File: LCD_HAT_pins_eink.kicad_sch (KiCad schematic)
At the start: 32 parts, among them J1 Qwiic, J2 LCD, J3 PWR_JUMPER, J4 PWR_JUMPER, J5 AFC24-S24FIC-00, Q1 Si1308, SW1 SW_Push, SW2 SW_Push, U1 SeeeduinoXIAO

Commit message: Rework routing
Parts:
- removed J4: PWR_JUMPER, Connector_PinHeader_2.54mm:PinHeader_1x02_P2.54mm_Vertical, symbol Connector:Conn_01x02_Pin
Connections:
- net +3.3V: now also J1.2 (Pin_2)
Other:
- title: Feather and Nano to LCD HAT -> Feather and Nano to LCD HAT + 24 pins SPI Eink
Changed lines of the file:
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@@
 	(paper "A4")
 	(title_block
-		(title "Feather and Nano to LCD HAT")
+		(title "Feather and Nano to LCD HAT + 24 pins SPI Eink")
 		(date "2023-01-30")
 		(rev "1.0")
 		(company "BitBank Software, Inc.")
-		(comment 1 "A convenient board to test SPI LCDs")
+		(comment 1 "A convenient board to test SPI LCDs and Eink")
+		(comment 2 "Fork of original idea by FASANI CORP.")
 	)
 	(text "PREVGL"
@@
 	(wire
 		(pts
-			(xy 26.67 107.95) (xy 40.64 107.95)
-		)
-		(stroke
-			(width 0)
-			(type default)
-		)
-	)
-	(wire
-		(pts
 			(xy 248.285 78.105) (xy 250.825 78.105)
 		)
@@
 	(wire
 		(pts
-			(xy 26.67 105.41) (xy 35.56 105.41)
-		)
-		(stroke
-			(width 0)
-			(type default)
-		)
-	)
-	(wire
-		(pts
 			(xy 31.75 82.55) (xy 54.61 82.55)
 		)
@@
 	(wire
 		(pts
+			(xy 35.56 92.075) (xy 39.37 92.075)
+		)
+		(stroke
+			(width 0)
+			(type default)
+		)
+	)
+	(wire
+		(pts
 			(xy 58.42 52.07) (xy 86.36 52.07)
 		)
@@
 	(wire
 		(pts
-			(xy 234.315 55.245) (xy 234.315 56.515)
+			(xy 35.56 87.63) (xy 35.56 92.075)
 		)
 		(stroke
@@
 	(wire
 		(pts
-			(xy 257.175 99.695) (xy 264.795 99.695)
+			(xy 234.315 55.245) (xy 234.315 56.515)
 		)
 		(stroke
@@
 	(wire
 		(pts
-			(xy 134.62 100.33) (xy 49.53 100.33)
+			(xy 257.175 99.695) (xy 264.795 99.695)
 		)
 		(stroke
@@
 	(wire
 		(pts
-			(xy 91.44 64.77) (xy 101.6 64.77)
+			(xy 134.62 100.33) (xy 49.53 100.33)
 		)
 		(stroke
@@
 	(wire
 		(pts
-			(xy 101.6 59.69) (xy 101.6 60.96)
+			(xy 91.44 64.77) (xy 101.6 64.77)
 		)
 		(stroke
@@
 	(wire
 		(pts
-			(xy 97.79 36.83) (xy 161.29 36.83)
+			(xy 101.6 59.69) (xy 101.6 60.96)
 		)
 		(stroke
@@
 	(wire
 		(pts
-			(xy 35.56 87.63) (xy 35.56 105.41)
+			(xy 97.79 36.83) (xy 161.29 36.83)
 		)
 		(stroke
@@
 	(symbol
 		(lib_id "power:+3.3V")
-		(at 40.64 107.95 0)
+		(at 39.37 92.075 0)
 		(unit 1)
 		(exclude_from_sim no)
@@
 		(fields_autoplaced yes)
 		(property "Reference" "#PWR02"
-			(at 40.64 111.76 0)
+			(at 39.37 95.885 0)
 			(effects
 				(font
@@
 		)
 		(property "Value" "+3.3V"
-			(at 40.64 102.87 0)
+			(at 39.37 86.995 0)
 			(effects
 				(font
@@
 		)
 		(property "Footprint" ""
-			(at 40.64 107.95 0)
+			(at 39.37 92.075 0)
 			(effects
 				(font
@@
 		)
 		(property "Datasheet" ""
-			(at 40.64 107.95 0)
+			(at 39.37 92.075 0)
 			(effects
 				(font
@@
 		)
 		(property "Description" ""
-			(at 40.64 107.95 0)
+			(at 39.37 92.075 0)
 			(effects
 				(font
@@
 					(unit 1)
 				)
-			)
-		)
-	)
-	(symbol
-		(lib_id "Connector:Conn_01x02_Pin")
-		(at 21.59 105.41 0)
-		(unit 1)
-		(exclude_from_sim no)
-		(in_bom yes)
-		(on_board yes)
-		(dnp no)
-		(fields_autoplaced yes)
-		(property "Reference" "J4"
-			(at 22.225 101.6 0)
-			(effects
-				(font
-					(size 1.27 1.27)
-				)
-			)
-		)
-		(property "Value" "PWR_JUMPER"
-			(at 22.225 104.14 0)
-			(effects
-				(font
-					(size 1.27 1.27)
-				)
-			)
-		)
-		(property "Footprint" "Connector_PinHeader_2.54mm:PinHeader_1x02_P2.54mm_Vertical"
-			(at 21.59 105.41 0)
-			(effects
-				(font
-					(size 1.27 1.27)
-				)
-				(hide yes)
-			)
-		)
-		(property "Datasheet" "~"
-			(at 21.59 105.41 0)
-			(effects
-				(font
-					(size 1.27 1.27)
-				)
-				(hide yes)
-			)
-		)
-		(property "Description" ""
-			(at 21.59 105.41 0)
-			(effects
-				(font
-					(size 1.27 1.27)
-				)
-			)
-		)
-		(pin "1"
-		)
-		(pin "2"
-		)
-		(instances
-			(project "LCD_HAT"
-				(path "/9ace1ea2-fe32-42b9-a35c-4c1c5b2f3f56"
-					(reference "J4")
-					(unit 1)
-				)

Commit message: FAB Files 1.0
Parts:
- removed J3: PWR_JUMPER, Connector_PinHeader_2.54mm:PinHeader_1x02_P2.54mm_Vertical, symbol Connector:Conn_01x02_Pin
- A1, A2, U1: now left out of the parts list
- J1: LCSC (none) -> C160404
- J5: LCSC (none) -> C262292
- R1, R2: LCSC (none) -> C25804
- R3: LCSC (none) -> C245058
- SW1, SW2: LCSC (none) -> C19190908
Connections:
- net +3.3V: now also J2.2 (Pin_2)
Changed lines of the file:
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@@
 	(wire
 		(pts
-			(xy 163.83 60.96) (xy 163.83 49.53)
+			(xy 163.83 40.64) (xy 163.83 60.96)
 		)
 		(stroke
@@
 	(wire
 		(pts
-			(xy 163.83 46.99) (xy 163.83 40.64)
-		)
-		(stroke
-			(width 0)
-			(type default)
-		)
-	)
-	(wire
-		(pts
 			(xy 146.05 68.58) (xy 167.64 68.58)
 		)
@@
 	(wire
 		(pts
-			(xy 165.1 46.99) (xy 163.83 46.99)
-		)
-		(stroke
-			(width 0)
-			(type default)
-		)
-	)
-	(wire
-		(pts
 			(xy 101.6 54.61) (xy 93.98 54.61)
 		)
@@
 	(wire
 		(pts
-			(xy 163.83 49.53) (xy 165.1 49.53)
-		)
-		(stroke
-			(width 0)
-			(type default)
-		)
-	)
-	(wire
-		(pts
 			(xy 82.55 115.57) (xy 82.55 109.22)
 		)
@@
 			)
 		)
+		(property "LCSC" "C19190908"
+			(at 100.33 115.57 0)
+			(effects
+				(font
+					(size 1.27 1.27)
+				)
+				(hide yes)
+			)
+		)
 		(pin "1"
 		)
@@
 		(unit 1)
 		(exclude_from_sim no)
-		(in_bom yes)
+		(in_bom no)
 		(on_board yes)
 		(dnp no)
@@
 	)
 	(symbol
-		(lib_id "Connector:Conn_01x02_Pin")
-		(at 170.18 49.53 180)
-		(unit 1)
-		(exclude_from_sim no)
-		(in_bom yes)
-		(on_board yes)
-		(dnp no)
-		(fields_autoplaced yes)
-		(property "Reference" "J3"
-			(at 171.45 47.625 0)
-			(effects
-				(font
-					(size 1.27 1.27)
-				)
-				(justify right)
-			)
-		)
-		(property "Value" "PWR_JUMPER"
-			(at 171.45 50.165 0)
-			(effects
-				(font
-					(size 1.27 1.27)
-				)
-				(justify right)
-			)
-		)
-		(property "Footprint" "Connector_PinHeader_2.54mm:PinHeader_1x02_P2.54mm_Vertical"
-			(at 170.18 49.53 0)
-			(effects
-				(font
-					(size 1.27 1.27)
-				)
-				(hide yes)
-			)
-		)
-		(property "Datasheet" "~"
-			(at 170.18 49.53 0)
-			(effects
-				(font
-					(size 1.27 1.27)
-				)
-				(hide yes)
-			)
-		)
-		(property "Description" ""
-			(at 170.18 49.53 0)
-			(effects
-				(font
-					(size 1.27 1.27)
-				)
-			)
-		)
-		(pin "1"
-		)
-		(pin "2"
-		)
-		(instances
-			(project "LCD_HAT"
-				(path "/9ace1ea2-fe32-42b9-a35c-4c1c5b2f3f56"
-					(reference "J3")
-					(unit 1)
-				)
-			)
-		)
-	)
-	(symbol
 		(lib_id "power:+3.3V")
 		(at 73.66 21.59 0)
@@
 			)
 		)
+		(property "LCSC" "C19190908"
+			(at 77.47 115.57 0)
+			(effects
+				(font
+					(size 1.27 1.27)
+				)
+				(hide yes)
+			)
+		)
 		(pin "1"
 		)
@@
 			)
 		)
+		(property "LCSC" "C25804"
+			(at 72.39 124.46 0)
+			(effects
+				(font
+					(size 1.27 1.27)
+				)
+				(hide yes)
+			)
+		)
 		(pin "1"
 		)
@@
 			)
 		)
-		(property "Datasheet" "C262292"
+		(property "Datasheet" ""
 			(at 206.375 121.285 0)
 			(effects
@@
 			)
 		)
+		(property "LCSC" "C262292"
+			(at 216.535 117.475 0)
+			(effects
+				(font
+					(size 1.27 1.27)
+				)
+				(hide yes)
+			)
+		)
 		(pin "1"
 		)
@@
 		(unit 1)
 		(exclude_from_sim no)
-		(in_bom yes)
+		(in_bom no)
 		(on_board yes)
 		(dnp no)
@@
 			)
 		)
+		(property "LCSC" "C25804"
+			(at 95.25 124.46 0)
+			(effects
+				(font
+					(size 1.27 1.27)
+				)
+				(hide yes)
+			)
+		)
 		(pin "1"
 		)
@@
 		(unit 1)
 		(exclude_from_sim no)
-		(in_bom yes)
+		(in_bom no)
 		(on_board yes)
 		(dnp no)
@@
 			)
 		)
+		(property "LCSC" "C160404"
+			(at 26.67 87.63 0)
+			(effects
+				(font
+					(size 1.27 1.27)
+				)
+				(hide yes)
+			)
+		)
 		(pin "1"
 		)
@@
 			)
 		)
+		(property "LCSC" "C245058"
+			(at 139.7 49.53 90)
+			(effects
+				(font
+					(size 1.27 1.27)
+				)
+				(hide yes)
+			)
+		)

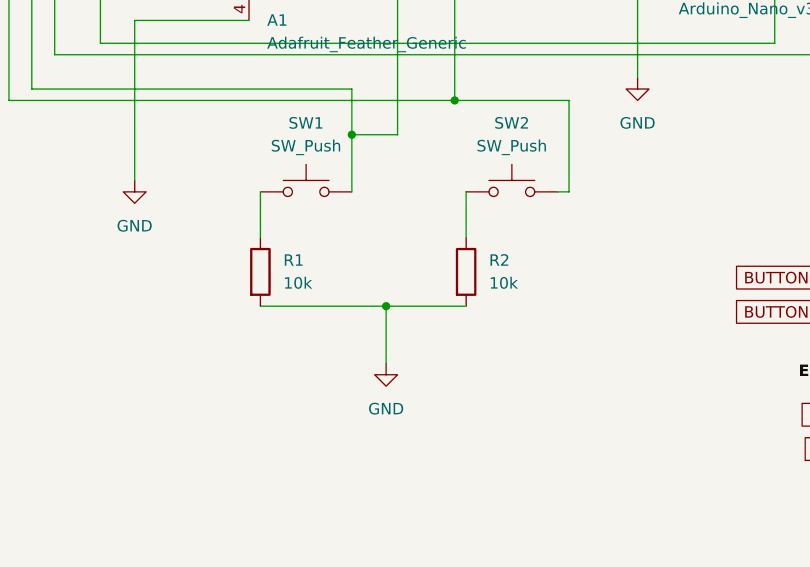
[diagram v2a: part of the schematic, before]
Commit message: FIX pin not connected to GND in 24 pin FPC
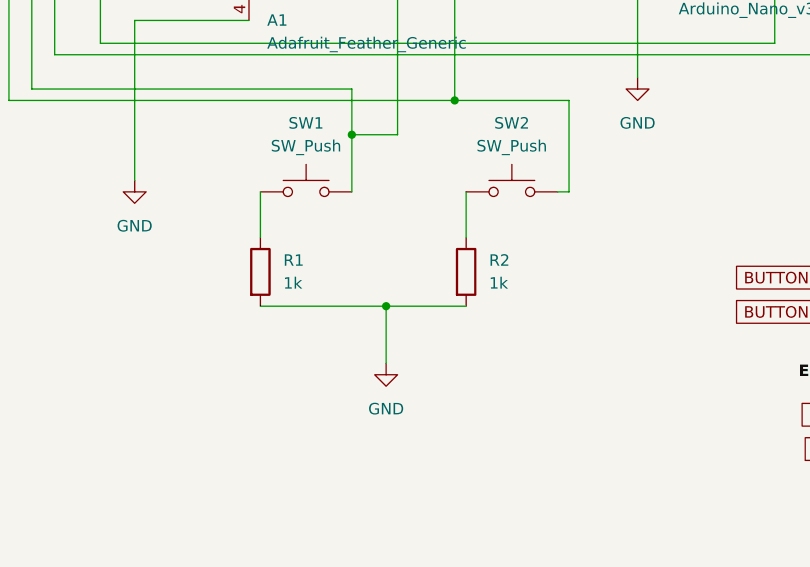
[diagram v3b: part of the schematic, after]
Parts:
- R1, R2: value 10k -> 1k; LCSC C25804 -> C11702
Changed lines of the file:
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@@
 			)
 		)
-		(property "Value" "10k"
+		(property "Value" "1k"
 			(at 74.93 125.7299 0)
 			(effects
@@
 			)
 		)
-		(property "LCSC" "C25804"
+		(property "LCSC" "C11702"
 			(at 72.39 124.46 0)
 			(effects
@@
 			)
 		)
-		(property "Value" "10k"
+		(property "Value" "1k"
 			(at 97.79 125.7299 0)
 			(effects
@@
 			)
 		)
-		(property "LCSC" "C25804"
+		(property "LCSC" "C11702"
 			(at 95.25 124.46 0)
 			(effects
